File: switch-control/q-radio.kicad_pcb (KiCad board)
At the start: 6 copper layers, 120 x 75 mm, 22 parts, among them U10 74LVC1G86, U11 74LVC1G86, U26 74HC00, U27 74LVC1G32, U39 74LVC1G08

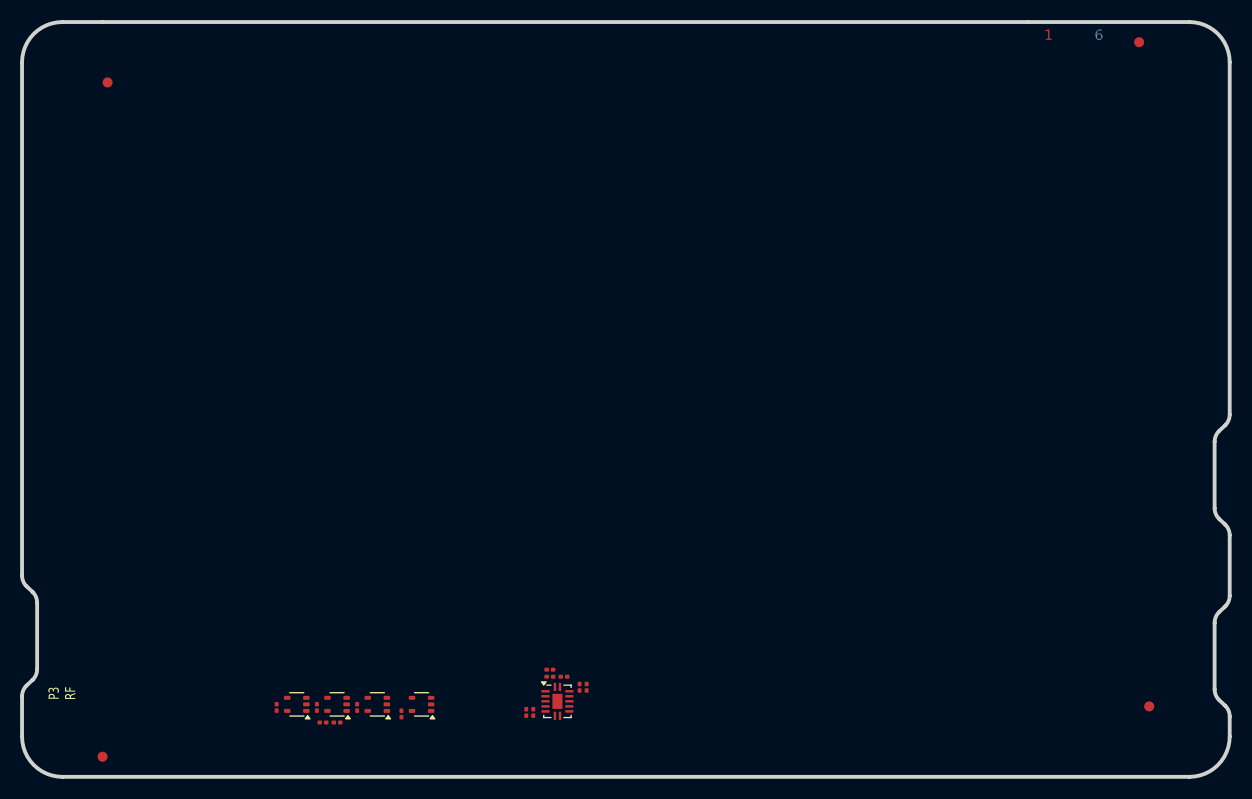
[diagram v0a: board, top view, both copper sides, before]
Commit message: Applied switch control candidate to sw submodule
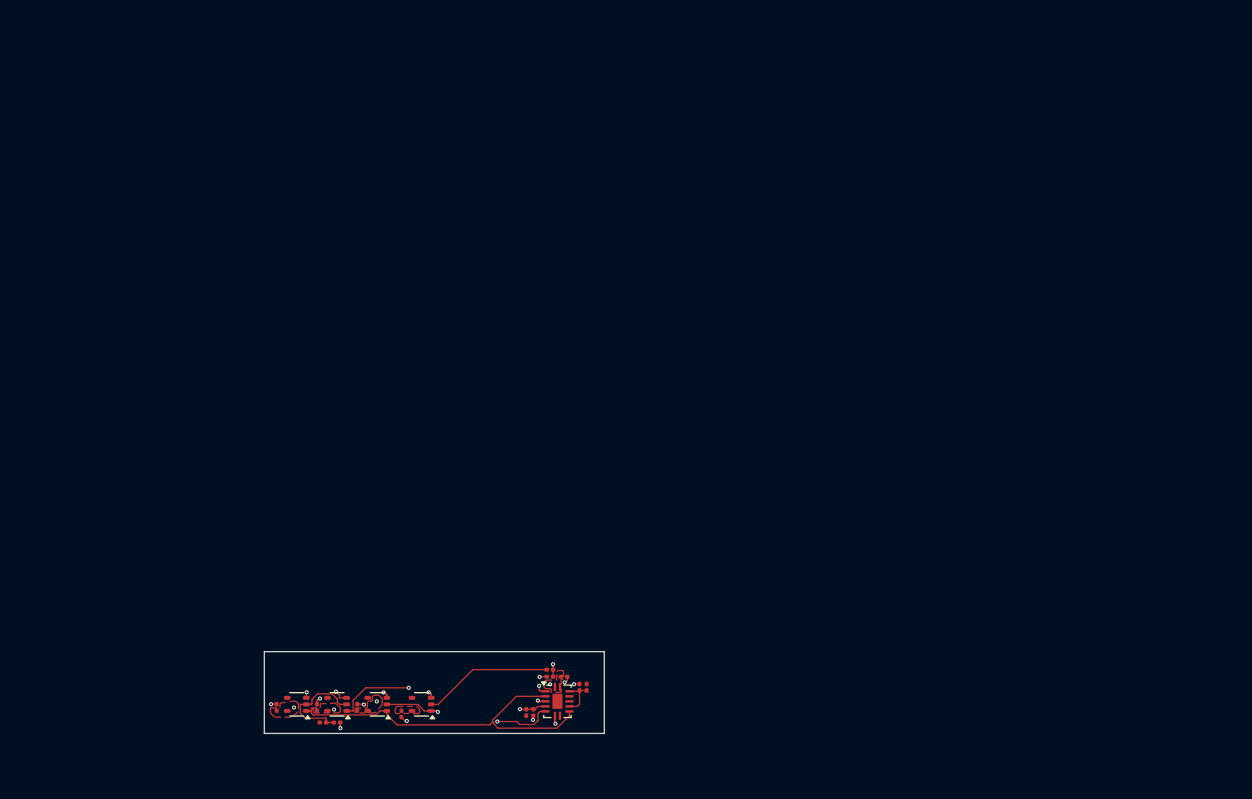
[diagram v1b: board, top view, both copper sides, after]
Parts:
- removed FID1, FID2, FID3, FID4: Fiducial_1mm_Mask2mm, Fiducial:Fiducial_1mm_Mask2mm
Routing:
- net /Switch Control/RX_EN: track 0.00 -> 35.2 mm
- net Net-(R94-Pad2): track 0.00 -> 22.3 mm, vias 0 -> 2
- net /Switch Control/MIX_EN: track 0.00 -> 17.5 mm, vias 0 -> 2
- net /Switch Control/TX_EN: track 0.00 -> 12.9 mm
- net Net-(R98-Pad2): track 0.00 -> 10.7 mm
- net GND: track 0.00 -> 10.0 mm, vias 0 -> 14
- net Net-(R24-Pad2): track 0.00 -> 5.05 mm, vias 0 -> 2
- net Net-(R96-Pad2): track 0.00 -> 4.20 mm
- net 2V5RF: track 0.00 -> 0.79 mm, vias 0 -> 5
- added copper zone on F.Cu, net 2V5RF
- added copper zone on In2.Cu, net 2V5RF
- added copper zone on In1.Cu, net GND
- added copper zone on In4.Cu, net GND
- added copper zone on F.Cu, net VAA
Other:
- board size 120 x 75 mm -> 33.8 x 8.1 mm
- board text removed: "1"
- board text removed: "2"
- board text removed: "3"
- board text removed: "4"
- board text removed: "5"
- board text removed: "6"
- board text removed: "P3 RF"
